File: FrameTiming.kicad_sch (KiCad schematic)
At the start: 12 parts, among them U20 74LS30, U25 74LS14, U59 74LS00, U64 74LS30, U65 74LS20, U66 74LS00, U67 74LS32, U68 74LS148, U69 74LS30

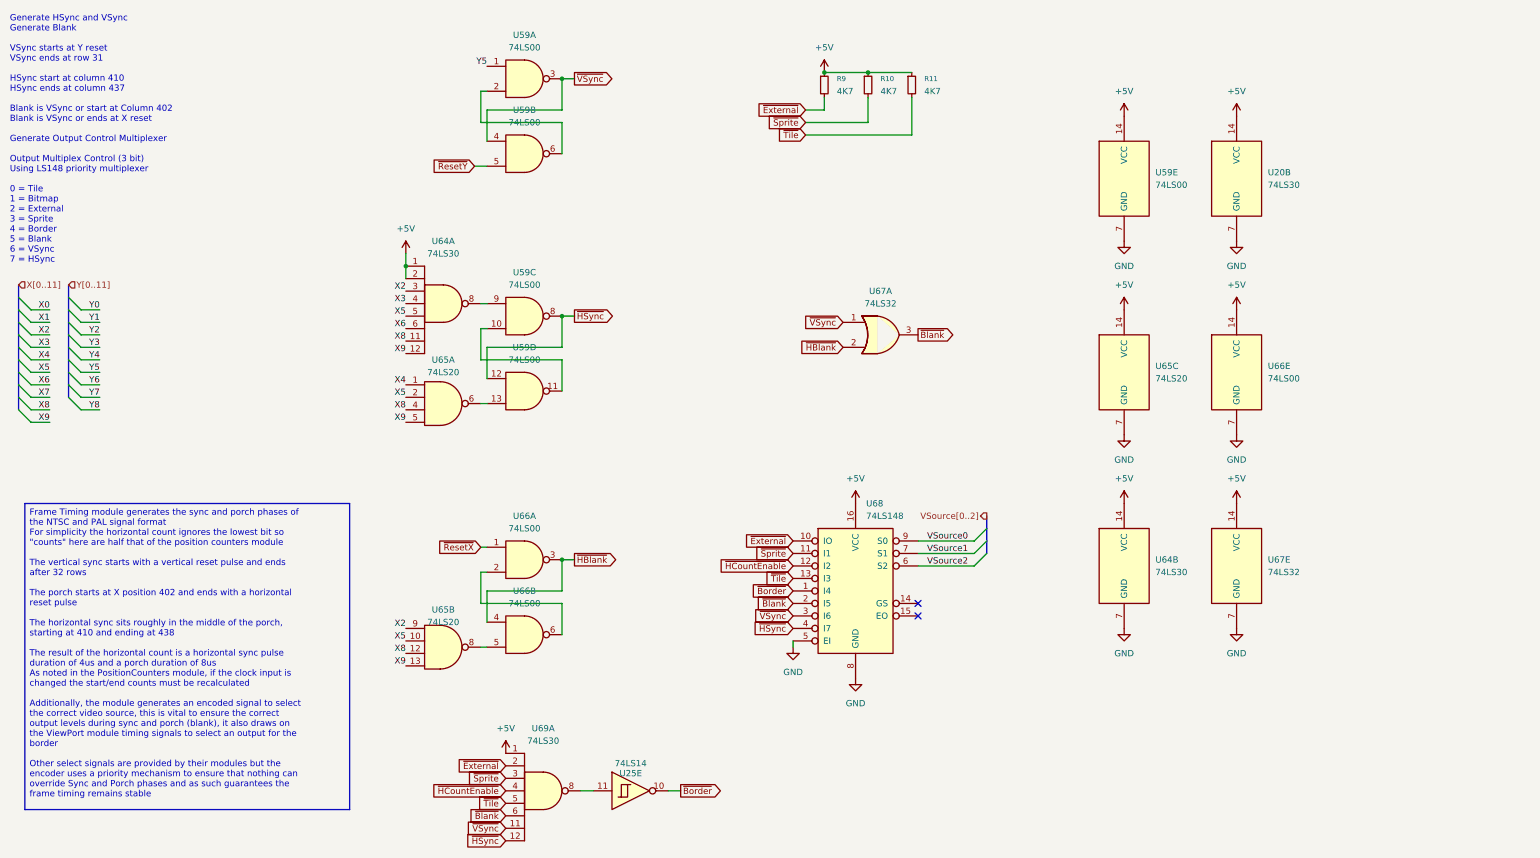
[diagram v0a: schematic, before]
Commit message: rework schematic isolation
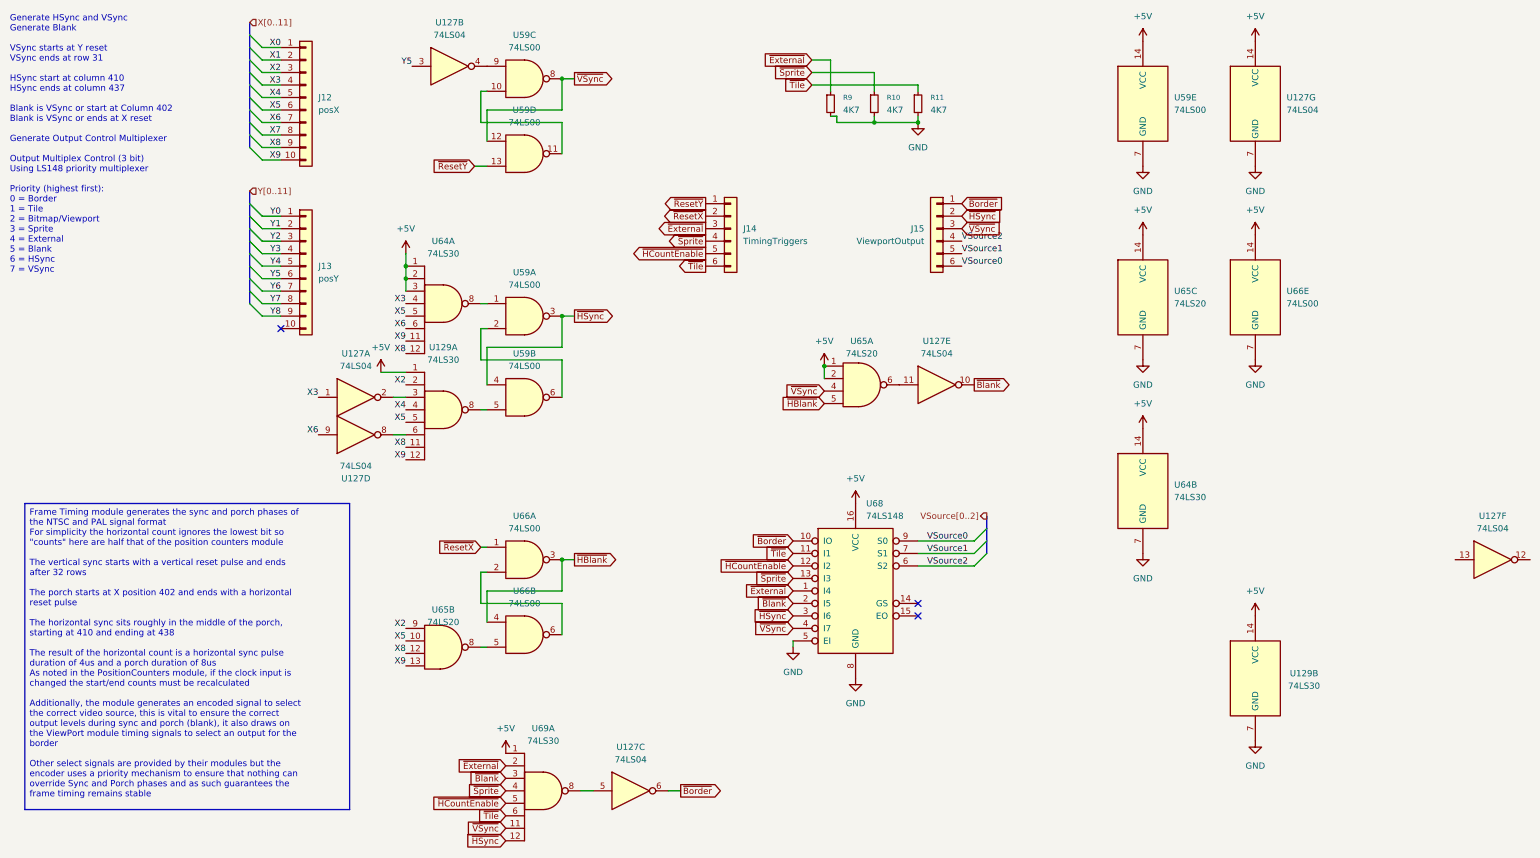
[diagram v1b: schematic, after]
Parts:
- removed U20: 74LS30, Package_SO:SO-14_3.9x8.65mm_P1.27mm, symbol 74xx:74LS30
- removed U25: 74LS14, Package_SO:SO-14_3.9x8.65mm_P1.27mm, symbol 74xx:74LS14
- removed U67: 74LS32, Package_SO:SO-14_3.9x8.65mm_P1.27mm, symbol 74xx:74LS32
- added J12: posX, Connector_PinSocket_2.54mm:PinSocket_1x10_P2.54mm_Vertical, symbol Connector_Generic:Conn_01x10
- added J13: posY, Connector_PinSocket_2.54mm:PinSocket_1x10_P2.54mm_Vertical, symbol Connector_Generic:Conn_01x10
- added J14: TimingTriggers, Connector_PinSocket_2.54mm:PinSocket_1x06_P2.54mm_Vertical, symbol Connector_Generic:Conn_01x06
- added J15: ViewportOutput, Connector_PinSocket_2.54mm:PinSocket_1x06_P2.54mm_Vertical, symbol Connector_Generic:Conn_01x06
- added U127: 74LS04, Package_SO:SOIC-14_3.9x8.7mm_P1.27mm, symbol 74xx:74LS04
- added U129: 74LS30, Package_SO:SO-14_3.9x8.65mm_P1.27mm, symbol 74xx:74LS30
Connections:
- net +5V: now also U64.3, U65.1, U65.2, U127.14 (VCC), U129.1, U129.14 (VCC); no longer R10.1, R11.1, R9.1
- net GND: now also R10.2, R11.2, R9.2, U127.7 (GND), U129.7 (GND)
- net VSource0: now also J15.6 (Pin_6)
- net VSource1: now also J15.5 (Pin_5)
- net VSource2: now also J15.4 (Pin_4)
- net X0: now also J12.1 (Pin_1)
- net X1: now also J12.2 (Pin_2)
- net X2: now also J12.3 (Pin_3), U129.2; no longer U64.3
- net X3: now also J12.4 (Pin_4), U127.1
- net X4: now also J12.5 (Pin_5), U129.4; no longer U65.1
- net X5: now also J12.6 (Pin_6), U129.5; no longer U65.2
- net X6: now also J12.7 (Pin_7), U127.9
- net X7: now also J12.8 (Pin_8)
- net X8: now also U64.12, J12.9 (Pin_9), U129.11; no longer U64.11, U65.4
- net X9: now also U64.11, J12.10 (Pin_10), U129.12; no longer U64.12, U65.5
- net Y0: now also J13.1 (Pin_1)
- net Y1: now also J13.2 (Pin_2)
- net Y2: now also J13.3 (Pin_3)
- net Y3: now also J13.4 (Pin_4)
- net Y4: now also J13.5 (Pin_5)
- net Y5: now also J13.6 (Pin_6), U127.3; no longer U59.1
- net Y6: now also J13.7 (Pin_7)
- net Y7: now also J13.8 (Pin_8)
- net Y8: now also J13.9 (Pin_9)
- net ~{Blank}: now also U69.3, U127.10; no longer U69.6
- net ~{Border}: now also U68.10 (IO), J15.1 (Pin_1), U127.6; no longer U68.1 (I4)
- net ~{External}: now also R9.1, U68.1 (I4), J14.3 (Pin_3); no longer R9.2, U68.10 (IO)
- net ~{HBlank}: now also U65.5
- net ~{HCountEnable}: now also U69.5, J14.5 (Pin_5); no longer U69.4
- net ~{HSync}: now also U59.3, U59.4, U68.3 (I6), J15.2 (Pin_2); no longer U59.12, U59.8, U68.4 (I7)
- net ~{ResetX}: now also J14.2 (Pin_2)
- net ~{ResetY}: now also U59.13, J14.1 (Pin_1); no longer U59.5
- net ~{Sprite}: now also R10.1, U68.13 (I3), U69.4, J14.4 (Pin_4); no longer R10.2, U68.11 (I1), U69.3
- net ~{Tile}: now also R11.1, U68.11 (I1), U69.6, J14.6 (Pin_6); no longer R11.2, U68.13 (I3), U69.5
- net ~{VSync}: now also U59.12, U59.8, U65.4, U68.4 (I7), J15.3 (Pin_3); no longer U59.3, U59.4, U68.3 (I6)
- net at U59.9: now also U127.4; no longer U64.8
- net at U69.8: now also U127.5
- net at U65.6: now also U127.11; no longer U59.13
- new net: U129.8, U59.5
- new net: U59.1, U64.8
- new net: U127.2, U129.3
- new net: U127.8, U129.6
- no-connect marks 2 -> 3
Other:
- note added: "Generate HSync and VSync Generate Blank VSync starts at Y reset VSync ends at row 31 HSync start at column 410 HSync ends at column 437 Blank is VSync or start at Column 402 Blank is VSync or ends at X reset Generate Output Control Multiplexer Output Multiplex Control (3 bit) Using LS148 priority multiplexer Priority (highest first): 0 = Border 1 = Tile 2 = Bitmap/Viewport 3 = Sprite 4 = External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"
- note removed: "Generate HSync and VSync Generate Blank VSync starts at Y reset VSync ends at row 31 HSync start at column 410 HSync ends at column 437 Blank is VSync or start at Column 402 Blank is VSync or ends at X reset Generate Output Control Multiplexer Output Multiplex Control (3 bit) Using LS148 priority multiplexer 0 = Tile 1 = Bitmap 2 = External 3 = Sprite 4 = Border 5 = Blank 6 = VSync 7 = HSync"
- moved on the sheet: R10, R11, R9, U59E, U64B, U65C, U66E

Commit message: refine main board layout
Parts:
- added J44: Power, Connector_PinSocket_2.54mm:PinSocket_1x04_P2.54mm_Vertical, symbol Connector_Generic:Conn_01x04
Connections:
- net +5V: now also J44.1 (Pin_1), J44.4 (Pin_4)
- net GND: now also J44.2 (Pin_2), J44.3 (Pin_3)
